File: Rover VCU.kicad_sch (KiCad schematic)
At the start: 0 parts

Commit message: feat: added mcu
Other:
- added sheet MCU (STM32G0B1.kicad_sch)
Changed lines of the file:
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@@
 	(generator_version "10.0")
 	(paper "A4")
+	(sheet
+		(at 137.16 80.01)
+		(size 26.67 30.48)
+		(exclude_from_sim no)
+		(in_bom yes)
+		(on_board yes)
+		(dnp no)
+		(fields_autoplaced yes)
+		(stroke
+			(width 0.1524)
+			(type solid)
+		)
+		(fill
+			(color 0 0 0 0)
+		)
+		(property "Sheetname" "MCU"
+			(at 137.16 79.2984 0)
+			(show_name no)
+			(do_not_autoplace no)
+			(effects
+				(font
+					(size 1.27 1.27)
+				)
+				(justify left bottom)
+			)
+		)
+		(property "Sheetfile" "STM32G0B1.kicad_sch"
+			(at 137.16 111.0746 0)
+			(show_name no)
+			(do_not_autoplace no)
+			(effects
+				(font
+					(size 1.27 1.27)
+				)
+				(justify left top)
+			)
+		)
+		(instances
+			(project "Rover VCU"
+				(path "/33c96268-4ca2-4a73-94d6-a3ed4f27d429"
+					(page "2")
+				)
+			)
+		)
+	)
 	(sheet_instances
 		(path "/"

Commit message: feat: completed h63 implementation
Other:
- added sheet PHY (eth_phy.kicad_sch)
- sheet MCU ports: added CAN1_RX, CAN1_TX, CAN2_RX, CAN2_TX, GND, RMII_CRS_DV, RMII_MDC, RMII_MDIO, RMII_REF_CLK, RMII_RXD0, RMII_RXD1, RMII_TXD0, RMII_TXD1, RMII_TX_EN, VBUS, VDD_3V3; removed none
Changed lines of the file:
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@@
 	(paper "A4")
 	(sheet
-		(at 137.16 80.01)
-		(size 26.67 30.48)
+		(at 165.1 76.2)
+		(size 25.4 25.4)
 		(exclude_from_sim no)
 		(in_bom yes)
@@
 			(color 0 0 0 0)
 		)
+		(property "Sheetname" "PHY"
+			(at 165.1 75.4884 0)
+			(show_name no)
+			(do_not_autoplace no)
+			(effects
+				(font
+					(size 1.27 1.27)
+				)
+				(justify left bottom)
+			)
+		)
+		(property "Sheetfile" "eth_phy.kicad_sch"
+			(at 165.1 102.1846 0)
+			(show_name no)
+			(do_not_autoplace no)
+			(effects
+				(font
+					(size 1.27 1.27)
+				)
+				(justify left top)
+			)
+		)
+		(instances
+			(project "Rover VCU"
+				(path "/33c96268-4ca2-4a73-94d6-a3ed4f27d429"
+					(page "3")
+				)
+			)
+		)
+	)
+	(sheet
+		(at 128.27 76.2)
+		(size 26.67 45.72)
+		(exclude_from_sim no)
+		(in_bom yes)
+		(on_board yes)
+		(dnp no)
+		(fields_autoplaced yes)
+		(stroke
+			(width 0.1524)
+			(type solid)
+		)
+		(fill
+			(color 0 0 0 0)
+		)
 		(property "Sheetname" "MCU"
-			(at 137.16 79.2984 0)
+			(at 128.27 75.4884 0)
 			(show_name no)
 			(do_not_autoplace no)
@@
 		)
 		(property "Sheetfile" "STM32G0B1.kicad_sch"
-			(at 137.16 111.0746 0)
+			(at 128.27 122.5046 0)
 			(show_name no)
 			(do_not_autoplace no)
@@
 			)
 		)
+		(pin "VDD_3V3" input
+			(at 128.27 78.74 180)
+			(effects
+				(font
+					(size 1.27 1.27)
+				)
+				(justify left)
+			)
+		)
+		(pin "VBUS" input
+			(at 128.27 81.28 180)
+			(effects
+				(font
+					(size 1.27 1.27)
+				)
+				(justify left)
+			)
+		)
+		(pin "RMII_CRS_DV" input
+			(at 154.94 78.74 0)
+			(effects
+				(font
+					(size 1.27 1.27)
+				)
+				(justify right)
+			)
+		)
+		(pin "GND" input
+			(at 128.27 119.38 180)
+			(effects
+				(font
+					(size 1.27 1.27)
+				)
+				(justify left)
+			)
+		)
+		(pin "RMII_MDIO" input
+			(at 154.94 81.28 0)
+			(effects
+				(font
+					(size 1.27 1.27)
+				)
+				(justify right)
+			)
+		)
+		(pin "RMII_TX_EN" input
+			(at 154.94 83.82 0)
+			(effects
+				(font
+					(size 1.27 1.27)
+				)
+				(justify right)
+			)
+		)
+		(pin "RMII_TXD0" input
+			(at 154.94 86.36 0)
+			(effects
+				(font
+					(size 1.27 1.27)
+				)
+				(justify right)
+			)
+		)
+		(pin "RMII_TXD1" input
+			(at 154.94 88.9 0)
+			(effects
+				(font
+					(size 1.27 1.27)
+				)
+				(justify right)
+			)
+		)
+		(pin "RMII_REF_CLK" input
+			(at 154.94 91.44 0)
+			(effects
+				(font
+					(size 1.27 1.27)
+				)
+				(justify right)
+			)
+		)
+		(pin "CAN2_TX" input
+			(at 154.94 119.38 0)
+			(effects
+				(font
+					(size 1.27 1.27)
+				)
+				(justify right)
+			)
+		)
+		(pin "RMII_MDC" input
+			(at 154.94 93.98 0)
+			(effects
+				(font
+					(size 1.27 1.27)
+				)
+				(justify right)
+			)
+		)
+		(pin "RMII_RXD1" input
+			(at 154.94 96.52 0)
+			(effects
+				(font
+					(size 1.27 1.27)
+				)
+				(justify right)
+			)
+		)
+		(pin "RMII_RXD0" input
+			(at 154.94 99.06 0)
+			(effects
+				(font
+					(size 1.27 1.27)
+				)
+				(justify right)
+			)
+		)
+		(pin "CAN1_TX" input
+			(at 154.94 109.22 0)
+			(effects
+				(font
+					(size 1.27 1.27)
+				)
+				(justify right)
+			)
+		)
+		(pin "CAN1_RX" input
+			(at 154.94 111.76 0)
+			(effects
+				(font
+					(size 1.27 1.27)
+				)
+				(justify right)
+			)
+		)
+		(pin "CAN2_RX" input
+			(at 154.94 116.84 0)
+			(effects
+				(font
+					(size 1.27 1.27)
+				)
+				(justify right)
+			)
+		)

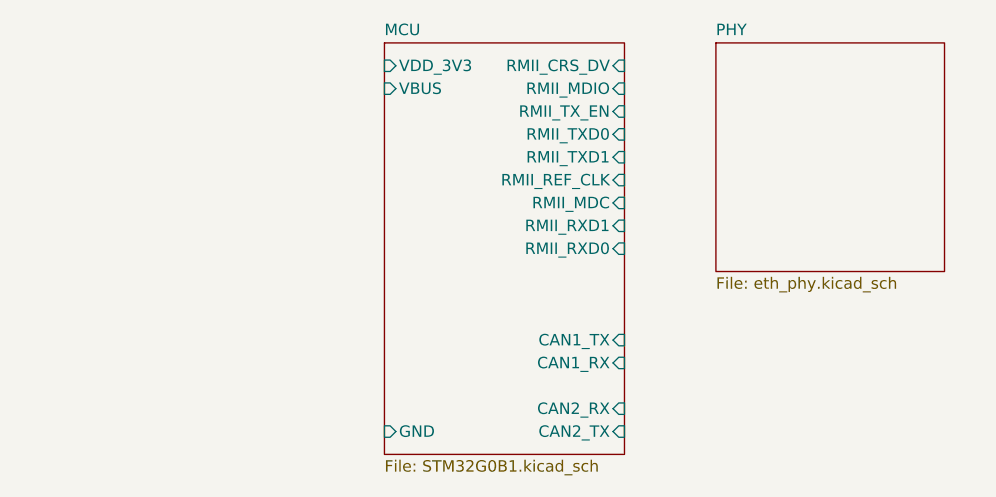
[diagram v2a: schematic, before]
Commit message: feat: added eth and can with
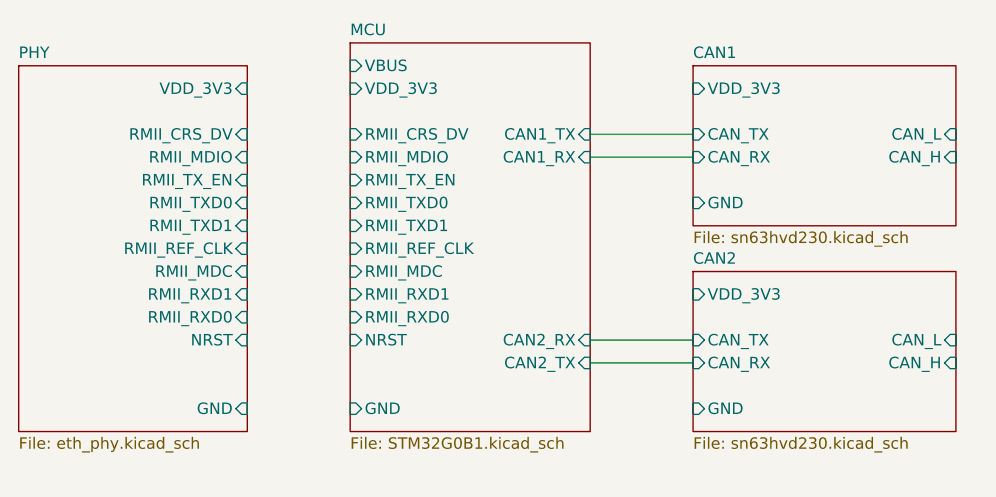
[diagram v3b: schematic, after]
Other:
- added sheet CAN1 (sn63hvd230.kicad_sch)
- added sheet CAN2 (sn63hvd230.kicad_sch)
- sheet MCU ports: added NRST; removed none
- sheet PHY ports: added GND, NRST, RMII_CRS_DV, RMII_MDC, RMII_MDIO, RMII_REF_CLK, RMII_RXD0, RMII_RXD1, RMII_TXD0, RMII_TXD1, RMII_TX_EN, VDD_3V3; removed none

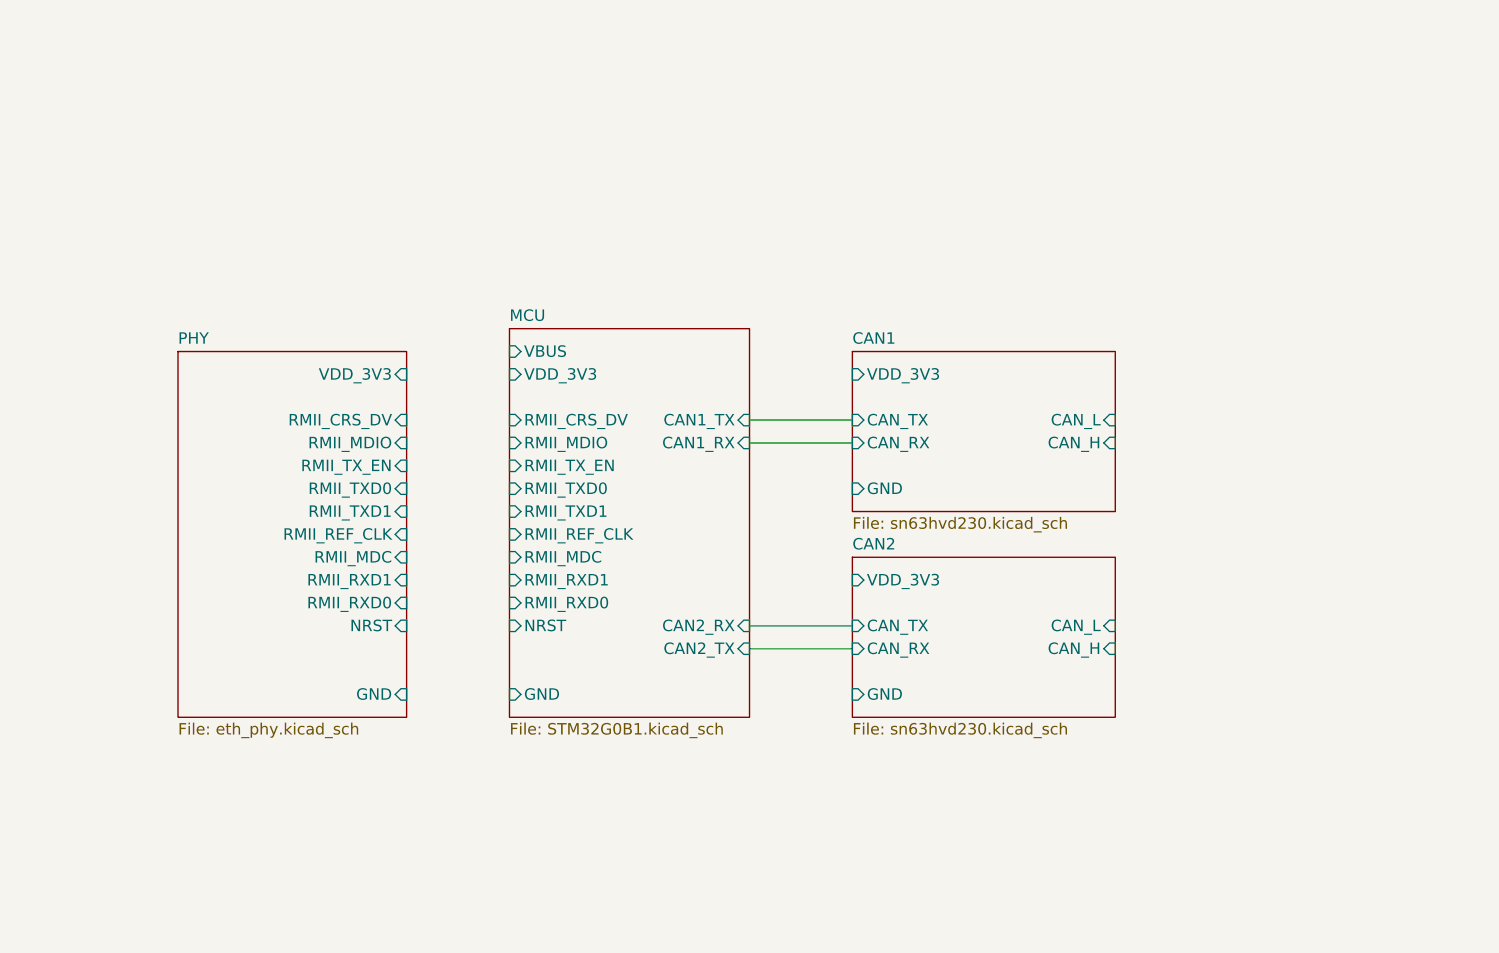
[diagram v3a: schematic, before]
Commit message: feat: added can bus channels and psu
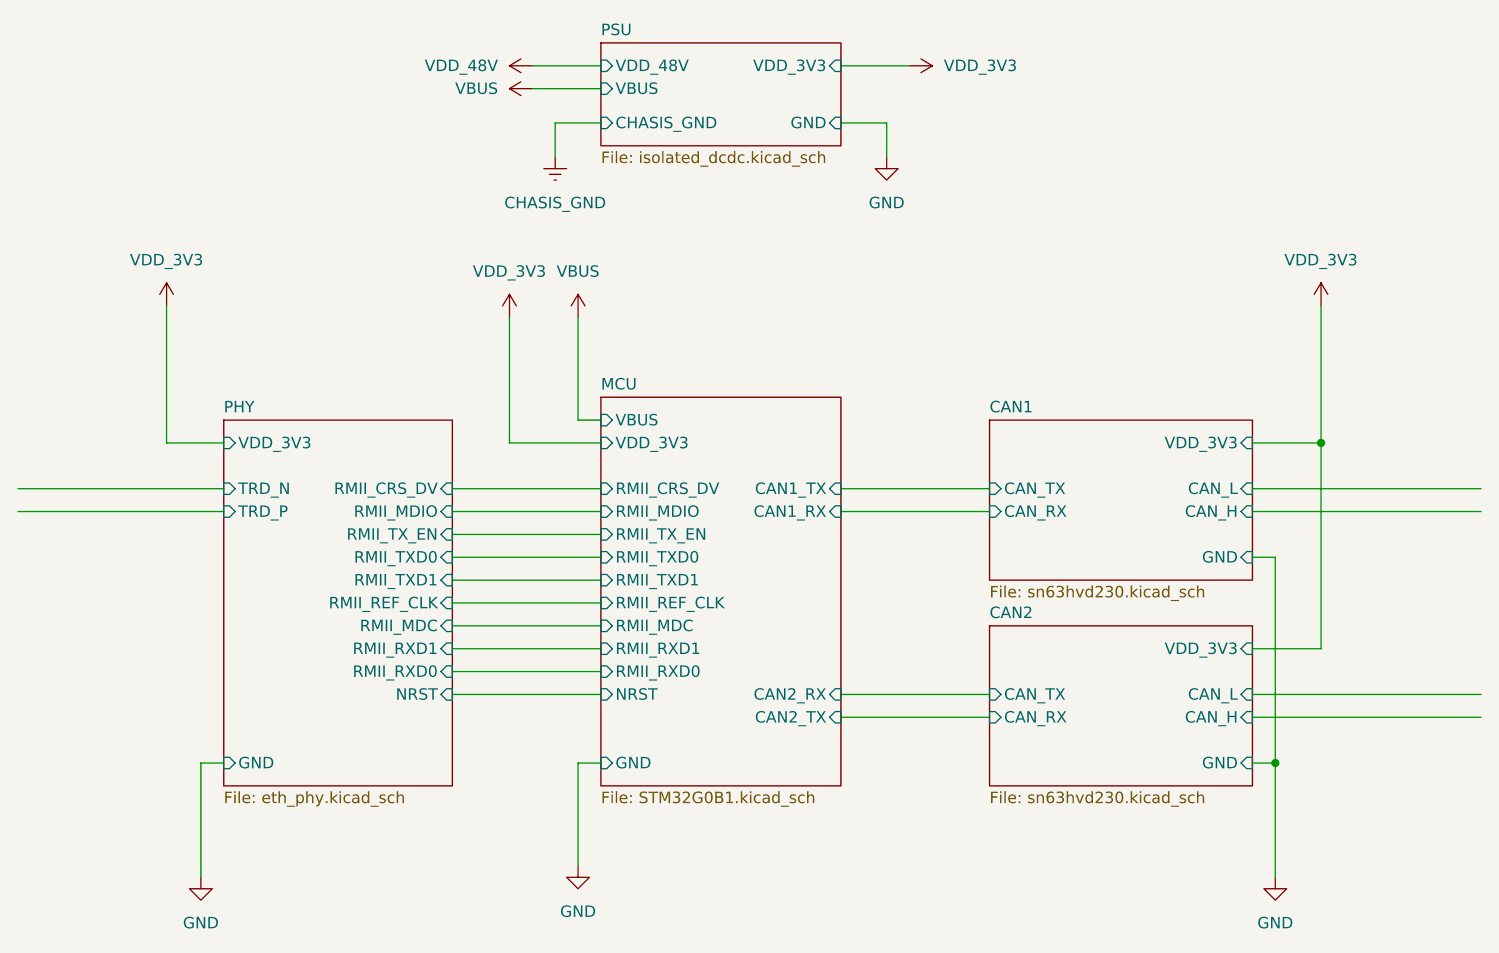
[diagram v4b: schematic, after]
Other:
- added sheet PSU (isolated_dcdc.kicad_sch)
- sheet PHY ports: added TRD_N, TRD_P; removed none

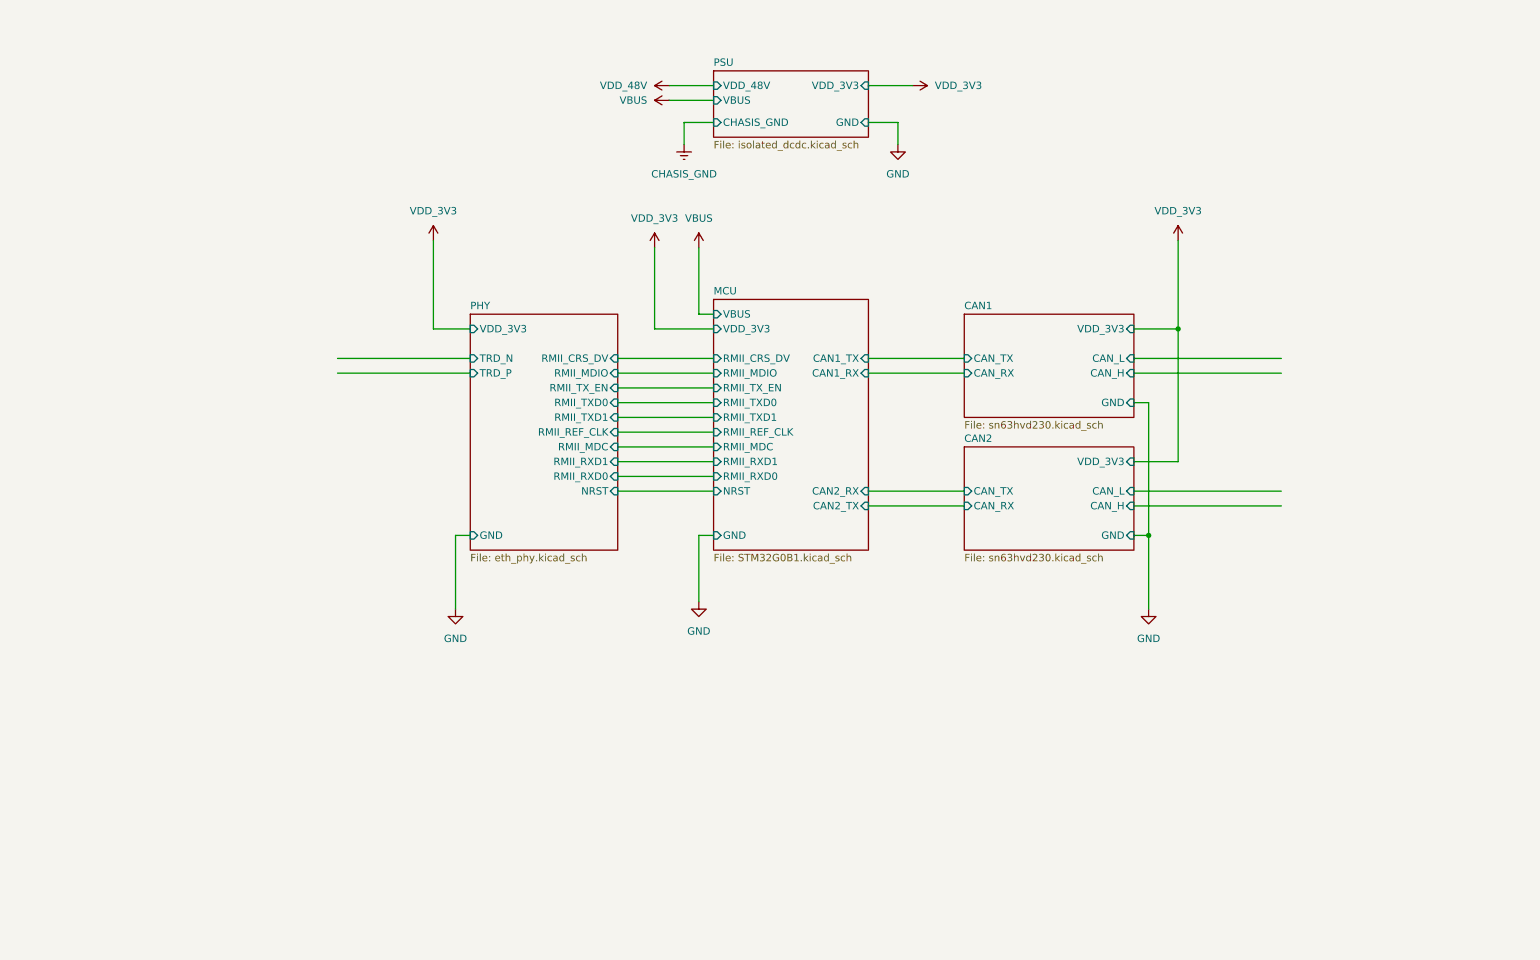
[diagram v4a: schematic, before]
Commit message: feat: added MVP routing implementation
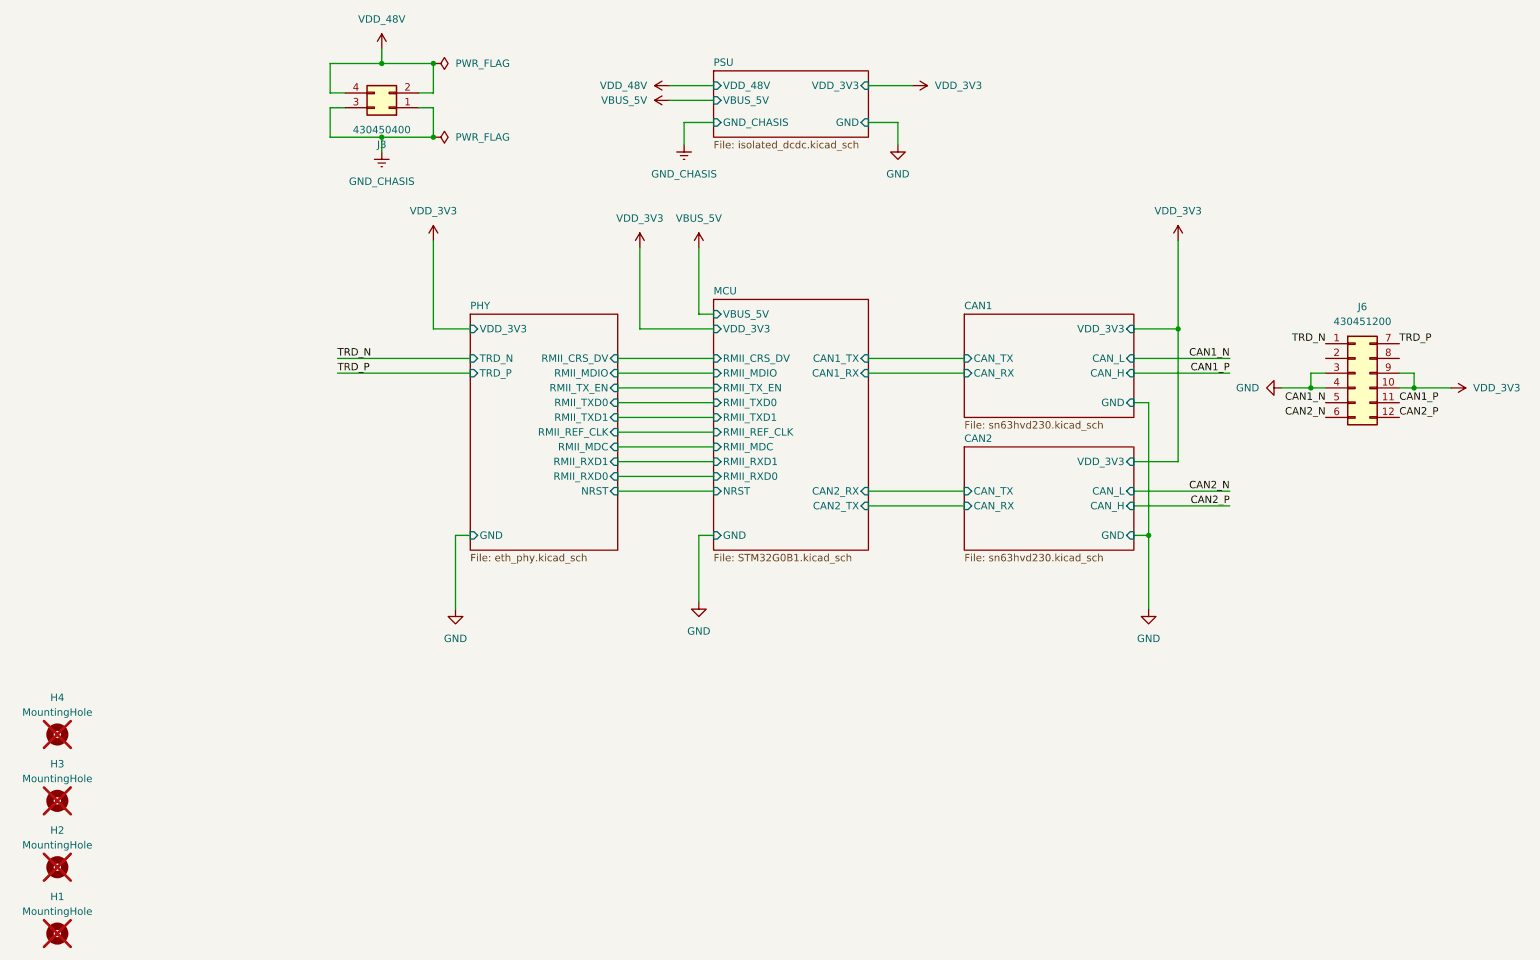
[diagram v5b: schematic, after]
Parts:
- added H1, H2, H3, H4: MountingHole, MountingHole:MountingHole_3.5mm, symbol Mechanical:MountingHole
- added J3: 430450400, Connector_Molex:Molex_Micro-Fit_3.0_43045-0400_2x02_P3.00mm_Horizontal, symbol 0_chenry_lib:430450400
- added J6: 430451200, Connector_Molex:Molex_Micro-Fit_3.0_43045-1221_2x06-1MP_P3.00mm_Horizontal, symbol 0_chenry_lib:430451200
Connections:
- net GND: now also J6.3 (Pin_3), J6.4 (Pin_4)
- net VDD_3V3: now also J6.10 (Pin_10), J6.9 (Pin_9)
- net VDD_48V: now also J3.2 (Pin_2), J3.4 (Pin_4)
- new net CAN1_N: J6.5 (Pin_5)
- new net CAN1_P: J6.11 (Pin_11)
- new net CAN2_N: J6.6 (Pin_6)
- new net CAN2_P: J6.12 (Pin_12)
- new net GND_CHASIS: J3.1 (Pin_1), J3.3 (Pin_3)
- new net TRD_N: J6.1 (Pin_1)
- new net TRD_P: J6.7 (Pin_7)
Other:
- sheet MCU ports: added VBUS_5V; removed VBUS
- sheet PSU ports: added GND_CHASIS, VBUS_5V; removed CHASIS_GND, VBUS
